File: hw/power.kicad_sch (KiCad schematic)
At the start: 48 parts, among them J9 Expansion, Q8 DMC2053UVT, U1 RT8096B, U2 RT8096B, U3 RT8096B, U5 TPS563249DDC

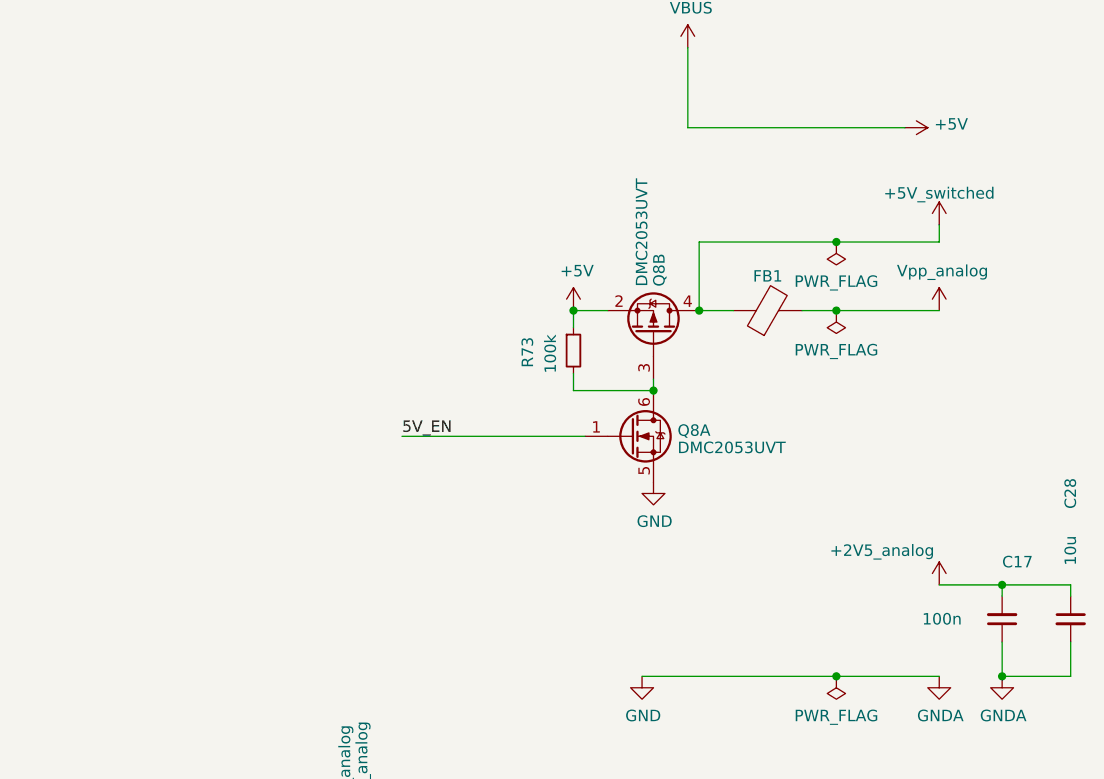
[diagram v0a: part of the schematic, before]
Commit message: Replaced 5V power switch by LDO.
Unregulated 5V introduced a LOT of noise into the FE.
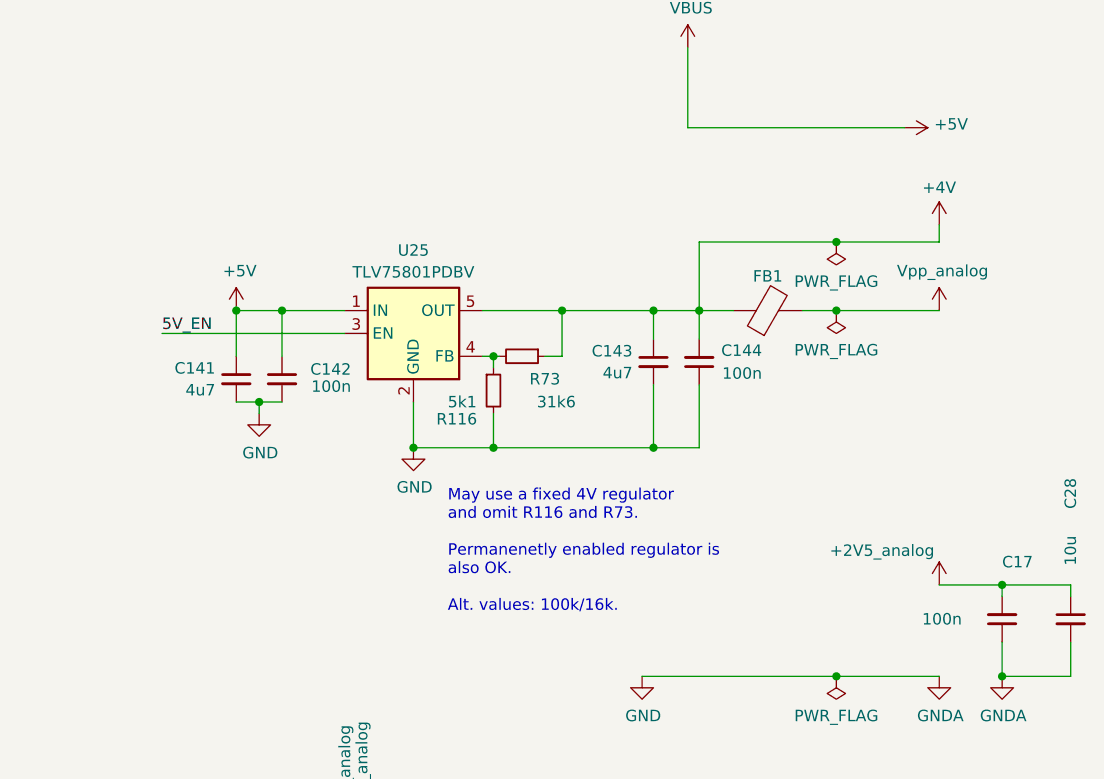
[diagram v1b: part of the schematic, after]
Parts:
- removed Q8: DMC2053UVT, Package_TO_SOT_SMD:TSOT-23-6, symbol Transistor_FET:DMC2053UVT
- added C141, C143: 4u7, Capacitor_SMD:C_0805_2012Metric, symbol Device:C_Small
- added C142, C144: 100n, Capacitor_SMD:C_0603_1608Metric, symbol Device:C_Small
- added R116: 5k1, Resistor_SMD:R_0603_1608Metric, symbol Device:R_Small
- added U25: TLV75801PDBV, Package_TO_SOT_SMD:SOT-23-5, symbol Regulator_Linear:TLV75801PDBV
- R73: value 100k -> 31k6
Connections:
- net +5V: now also C141.1, C142.1, U25.1 (IN); no longer R73.1
- net 5V_EN: now also U25.3 (EN)
- net GND: now also C141.2, C142.2, C143.2, C144.1, R116.2, U25.2 (GND)
- net at R73.2: now also R116.1, U25.4 (FB)
- net +5V_switched renamed +4V
- net +4V: now also R73.1, C143.1, C144.2, U25.5 (OUT)
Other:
- note added: "May use a fixed 4V regulator and omit R116 and R73. Permanenetly enabled regulator is also OK. Alt. values: 100k/16k."

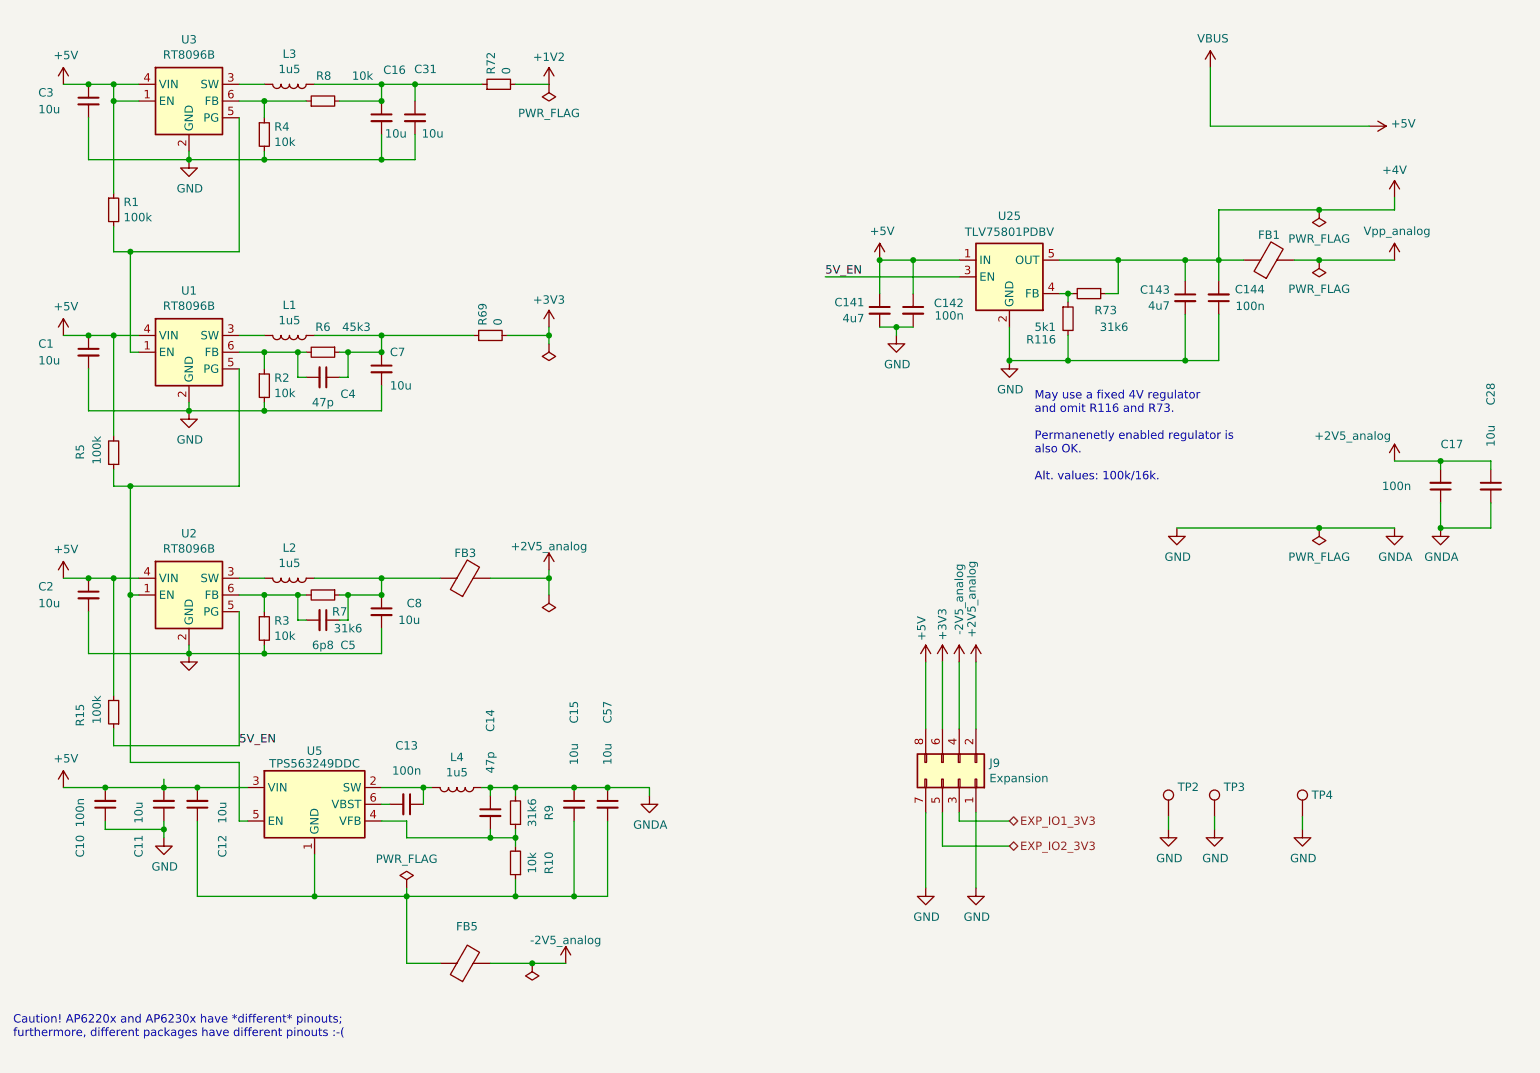
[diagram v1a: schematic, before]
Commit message: added jumperable VDDIO for digital I/O, added reset generator
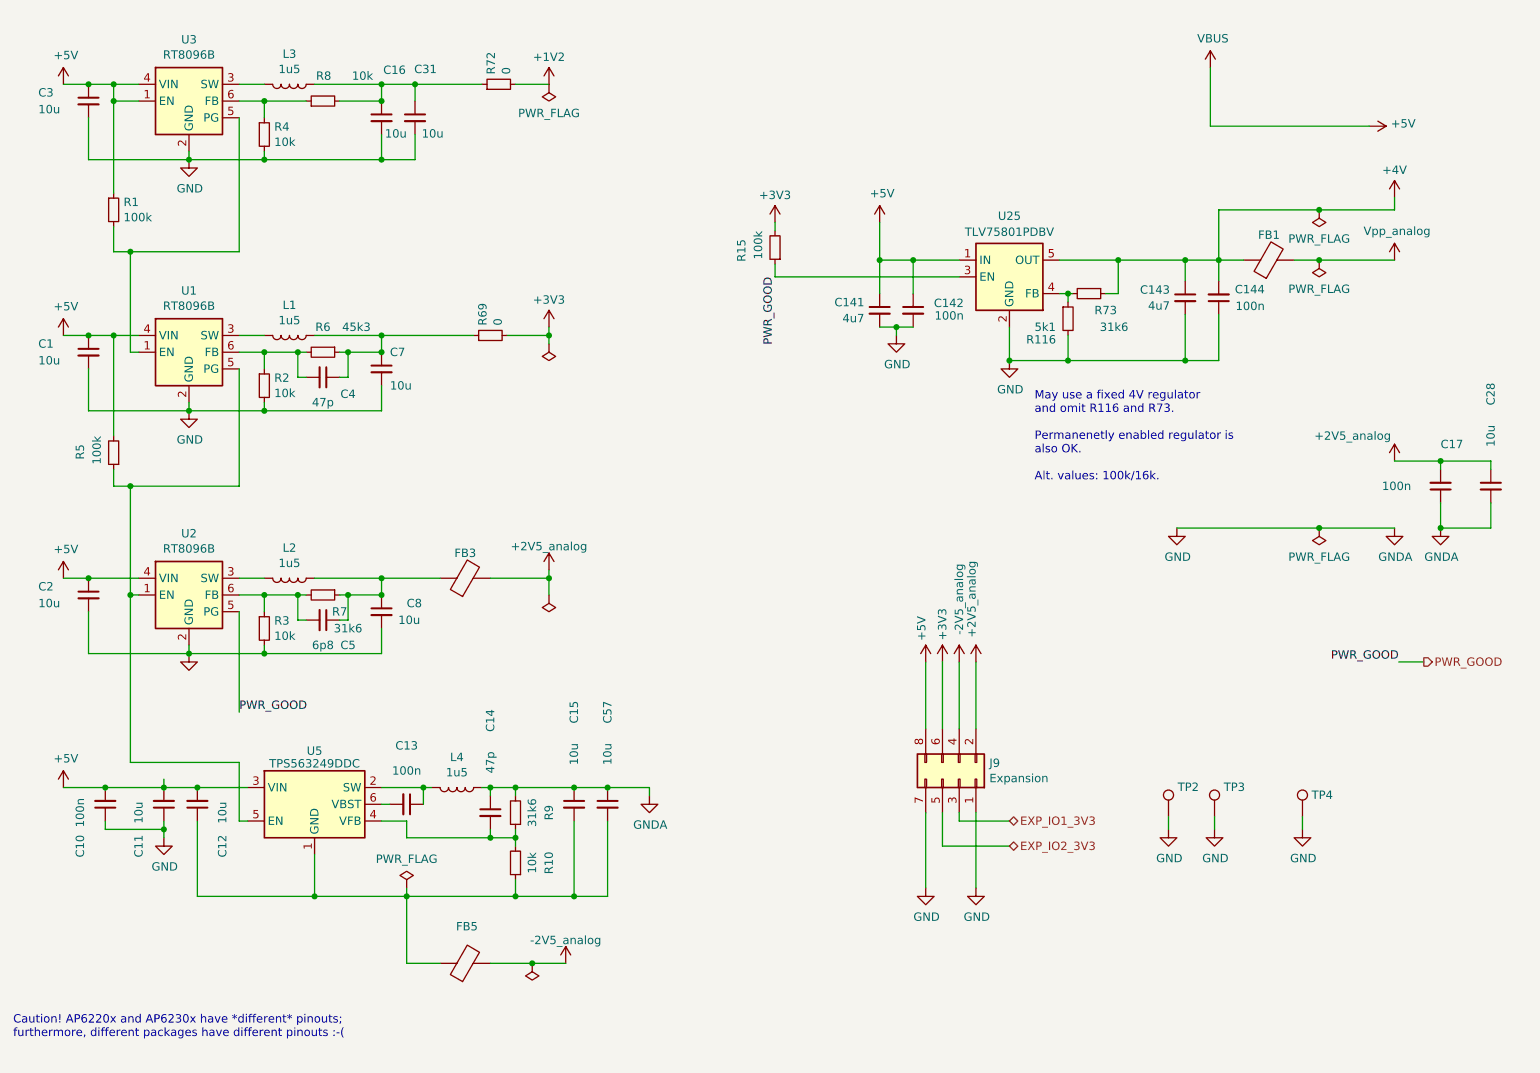
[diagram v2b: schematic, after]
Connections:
- net +3V3: now also R15.2
- net +5V: no longer R15.2
- net 5V_EN renamed PWR_GOOD
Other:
- moved on the sheet: R15
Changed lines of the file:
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@@
   (junction (at 66.04 138.43) (diameter 0) (color 0 0 0 0)
   )
-  (junction (at 58.42 106.68) (diameter 0) (color 0 0 0 0)
-  )
   (junction (at 259.715 88.9) (diameter 0) (color 0 0 0 0)
   )
@@
     (stroke (width 0) (type default))
   )
+  (wire (pts (xy 158.75 60.96) (xy 186.69 60.96))
+    (stroke (width 0) (type default))
+  )
   (wire (pts (xy 54.61 69.85) (xy 50.8 69.85))
     (stroke (width 0) (type default))
@@
     (stroke (width 0) (type default))
   )
+  (wire (pts (xy 253.365 119.38) (xy 257.175 119.38))
+    (stroke (width 0) (type default))
+  )
   (wire (pts (xy 99.06 39.37) (xy 99.06 43.18))
     (stroke (width 0) (type default))
   )
-  (wire (pts (xy 166.37 60.96) (xy 186.69 60.96))
-    (stroke (width 0) (type default))
-  )
   (wire (pts (xy 119.38 144.78) (xy 119.38 146.05))
     (stroke (width 0) (type default))
@@
     (stroke (width 0) (type default))
   )
-  (wire (pts (xy 77.47 132.08) (xy 77.47 111.76))
+  (wire (pts (xy 77.47 127) (xy 77.47 111.76))
     (stroke (width 0) (type default))
   )
@@
     (stroke (width 0) (type default))
   )
-  (wire (pts (xy 54.61 106.68) (xy 58.42 106.68))
+  (wire (pts (xy 54.61 106.68) (xy 62.23 106.68))
     (stroke (width 0) (type default))
   )
@@
     (stroke (width 0) (type default))
   )
+  (wire (pts (xy 174.625 52.705) (xy 174.625 58.42))
+    (stroke (width 0) (type default))
+  )
   (wire (pts (xy 119.38 31.75) (xy 124.46 31.75))
     (stroke (width 0) (type default))
@@
     (stroke (width 0) (type default))
   )
-  (wire (pts (xy 58.42 132.08) (xy 77.47 132.08))
-    (stroke (width 0) (type default))
-  )
   (wire (pts (xy 62.23 72.39) (xy 60.96 72.39))
     (stroke (width 0) (type default))
@@
     (stroke (width 0) (type default))
   )
+  (wire (pts (xy 158.75 52.705) (xy 158.75 53.975))
+    (stroke (width 0) (type default))
+  )
   (wire (pts (xy 66.04 144.78) (xy 66.04 143.51))
     (stroke (width 0) (type default))
@@
     (stroke (width 0) (type default))
   )
-  (wire (pts (xy 58.42 106.68) (xy 62.23 106.68))
-    (stroke (width 0) (type default))
-  )
   (wire (pts (xy 54.61 36.83) (xy 54.61 43.18))
     (stroke (width 0) (type default))
@@
     (stroke (width 0) (type default))
   )
-  (wire (pts (xy 58.42 106.68) (xy 58.42 124.46))
-    (stroke (width 0) (type default))
-  )
-  (wire (pts (xy 58.42 129.54) (xy 58.42 132.08))
+  (wire (pts (xy 158.75 59.055) (xy 158.75 60.96))
     (stroke (width 0) (type default))
   )
@@
     (effects (font (size 1.27 1.27)) (justify left bottom))
   )
-  (label "5V_EN" (at 77.47 132.08 0) (fields_autoplaced)
+  (label "PWR_GOOD" (at 77.47 127 0) (fields_autoplaced)
     (effects (font (size 1.27 1.27)) (justify left bottom))
   )
-  (label "5V_EN" (at 166.37 60.96 0) (fields_autoplaced)
-    (effects (font (size 1.27 1.27)) (justify left bottom))
+  (label "PWR_GOOD" (at 253.365 119.38 180) (fields_autoplaced)
+    (effects (font (size 1.27 1.27)) (justify right bottom))
+  )
+  (label "PWR_GOOD" (at 158.75 60.96 270) (fields_autoplaced)
+    (effects (font (size 1.27 1.27)) (justify right bottom))
+  )
+  (hierarchical_label "PWR_GOOD" (shape output) (at 257.175 119.38 0) (fields_autoplaced)
+    (effects (font (size 1.27 1.27)) (justify left))
   )
   (hierarchical_label "EXP_IO1_3V3" (shape bidirectional) (at 194.31 143.51 0) (fields_autoplaced)
@@
     )
   )
-  (symbol (lib_id "power:+5V") (at 174.625 58.42 0) (unit 1)
-    (in_bom yes) (on_board yes) (dnp no)
-    (property "Reference" "#PWR0164" (at 174.625 62.23 0)
-      (effects (font (size 1.27 1.27)) hide)
-    )
-    (property "Value" "+5V" (at 175.006 54.0258 0)
-      (effects (font (size 1.27 1.27)))
-    )
-    (property "Footprint" "" (at 174.625 58.42 0)
-      (effects (font (size 1.27 1.27)) hide)
-    )
-    (property "Datasheet" "" (at 174.625 58.42 0)
+  (symbol (lib_id "power:+5V") (at 174.625 52.705 0) (unit 1)
+    (in_bom yes) (on_board yes) (dnp no)
+    (property "Reference" "#PWR0164" (at 174.625 56.515 0)
+      (effects (font (size 1.27 1.27)) hide)
+    )
+    (property "Value" "+5V" (at 175.006 48.3108 0)
+      (effects (font (size 1.27 1.27)))
+    )
+    (property "Footprint" "" (at 174.625 52.705 0)
+      (effects (font (size 1.27 1.27)) hide)
+    )
+    (property "Datasheet" "" (at 174.625 52.705 0)
       (effects (font (size 1.27 1.27)) hide)
     )
@@
     )
   )
+  (symbol (lib_id "power:+3V3") (at 158.75 52.705 0) (unit 1)
+    (in_bom yes) (on_board yes) (dnp no) (fields_autoplaced)
+    (property "Reference" "#PWR0127" (at 158.75 56.515 0)
+      (effects (font (size 1.27 1.27)) hide)
+    )
+    (property "Value" "+3V3" (at 158.75 48.5719 0)
+      (effects (font (size 1.27 1.27)))
+    )
+    (property "Footprint" "" (at 158.75 52.705 0)
+      (effects (font (size 1.27 1.27)) hide)
+    )
+    (property "Datasheet" "" (at 158.75 52.705 0)
+      (effects (font (size 1.27 1.27)) hide)
+    )
+    (pin "1")
+    (instances
+      (project "usbadc"
+        (path "/7c8a1f8d-8834-4c9b-aaae-1f231e9b09a1/00000000-0000-0000-0000-00006086f2e3"
+          (reference "#PWR0127") (unit 1)
+        )
+      )
+    )
+  )
   (symbol (lib_id "Device:L") (at 110.49 138.43 270) (unit 1)
     (in_bom yes) (on_board yes) (dnp no)
@@
     )
   )
-  (symbol (lib_id "Device:R_Small") (at 58.42 127 180) (unit 1)
-    (in_bom yes) (on_board yes) (dnp no)
-    (property "Reference" "R15" (at 53.34 125.73 90)
-      (effects (font (size 1.27 1.27)) (justify left))
-    )
-    (property "Value" "100k" (at 55.88 124.46 90)
-      (effects (font (size 1.27 1.27)) (justify left))
-    )
-    (property "Footprint" "Resistor_SMD:R_0603_1608Metric" (at 58.42 127 0)
-      (effects (font (size 1.27 1.27)) hide)
-    )
-    (property "Datasheet" "~" (at 58.42 127 0)
-      (effects (font (size 1.27 1.27)) hide)
-    )
-    (property "Part" "" (at 58.42 127 0)
-      (effects (font (size 1.27 1.27)) hide)
-    )
-    (property "Manufacturer" "" (at 58.42 127 0)
-      (effects (font (size 1.27 1.27)) hide)
-    )
+  (symbol (lib_id "Device:R_Small") (at 158.75 56.515 180) (unit 1)
+    (in_bom yes) (on_board yes) (dnp no)
+    (property "Reference" "R15" (at 153.67 55.245 90)
+      (effects (font (size 1.27 1.27)) (justify left))
+    )
+    (property "Value" "100k" (at 156.21 53.975 90)
+      (effects (font (size 1.27 1.27)) (justify left))
+    )
+    (property "Footprint" "Resistor_SMD:R_0603_1608Metric" (at 158.75 56.515 0)
+      (effects (font (size 1.27 1.27)) hide)
+    )
+    (property "Datasheet" "~" (at 158.75 56.515 0)
+      (effects (font (size 1.27 1.27)) hide)
+    )
+    (property "Part" "" (at 158.75 56.515 0)
+      (effects (font (size 1.27 1.27)) hide)
+    )
+    (property "Manufacturer" "" (at 158.75 56.515 0)
+      (effects (font (size 1.27 1.27)) hide)
+    )

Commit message: Modified DAC resistors/range; connect + pull-up ADC SHDN
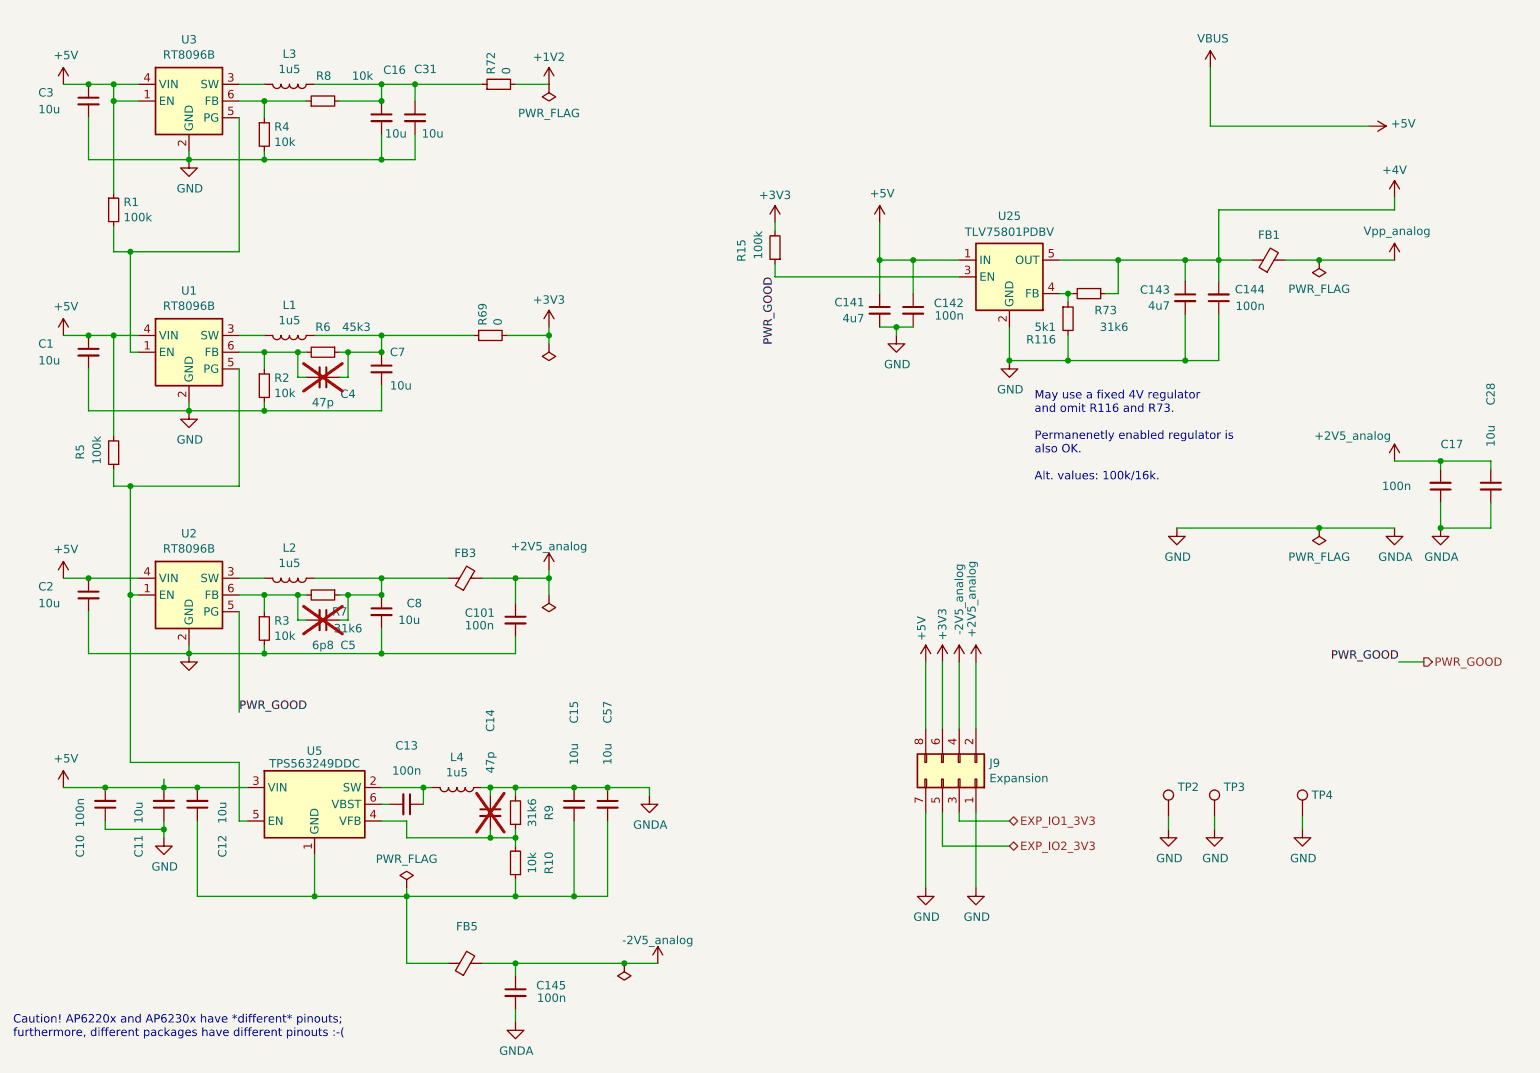
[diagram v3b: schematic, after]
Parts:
- added C101, C145: 100n, Capacitor_SMD:C_0603_1608Metric, symbol Device:C_Small
- C14, C4, C5: now not fitted; now left out of the parts list
- FB1, FB3, FB5: symbol Device:FerriteBead -> Device:FerriteBead_Small
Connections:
- net +2V5_analog: now also C101.1
- net -2V5_analog: now also C145.1
- net GND: now also C101.2, C145.2
